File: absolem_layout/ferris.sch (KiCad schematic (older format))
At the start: 100 parts, among them J1 USB C, K0_0 KEYSW, K0_1 KEYSW, K0_2 KEYSW, K0_3 KEYSW, K0_4 KEYSW, K0_5 KEYSW, K0_6 KEYSW, K0_7 KEYSW, K0_8 KEYSW, K0_9 KEYSW, K1_0 KEYSW, K1_1 KEYSW, K1_2 KEYSW, K1_3 KEYSW, K1_4 KEYSW, K1_5 KEYSW, K1_6 KEYSW, K1_7 KEYSW, K1_8 KEYSW, K1_9 KEYSW, K2_0 KEYSW, K2_1 KEYSW, K2_2 KEYSW, K2_3 KEYSW, K2_4 KEYSW, K2_5 KEYSW, K2_6 KEYSW, K2_7 KEYSW, K2_8 KEYSW, K2_9 KEYSW, K3_2 KEYSW, K3_3 KEYSW, K3_4 KEYSW, K3_5 KEYSW, K3_6 KEYSW, K3_7 KEYSW, SW1 SW_PUSH, U1 ATmega32U4-AU, U3 PCA9539PW, Y1 Crystal

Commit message: Fixed some staggering
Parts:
- removed C10, C9: 0.1u, Capacitor_SMD:C_0805_2012Metric_Pad1.15x1.40mm_HandSolder, symbol Device:C_Small
- removed Jack0, Jack1: TRRS, kbd:TRRS-PJ-320A, symbol Connector:AudioJack4
- removed R7, R8: 4.7k, Resistor_SMD:R_0805_2012Metric_Pad1.15x1.40mm_HandSolder, symbol Device:R
- removed R9: 10k, Resistor_SMD:R_0805_2012Metric_Pad1.15x1.40mm_HandSolder, symbol Device:R
- removed U3: PCA9539PW, Package_SO:TSSOP-24_4.4x7.8mm_P0.65mm, symbol ferris-rescue:PCA9539PW-Interface_Expansion-ferris-rescue
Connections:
- wire segments 137 -> 107
- no-connect marks 18 -> 10

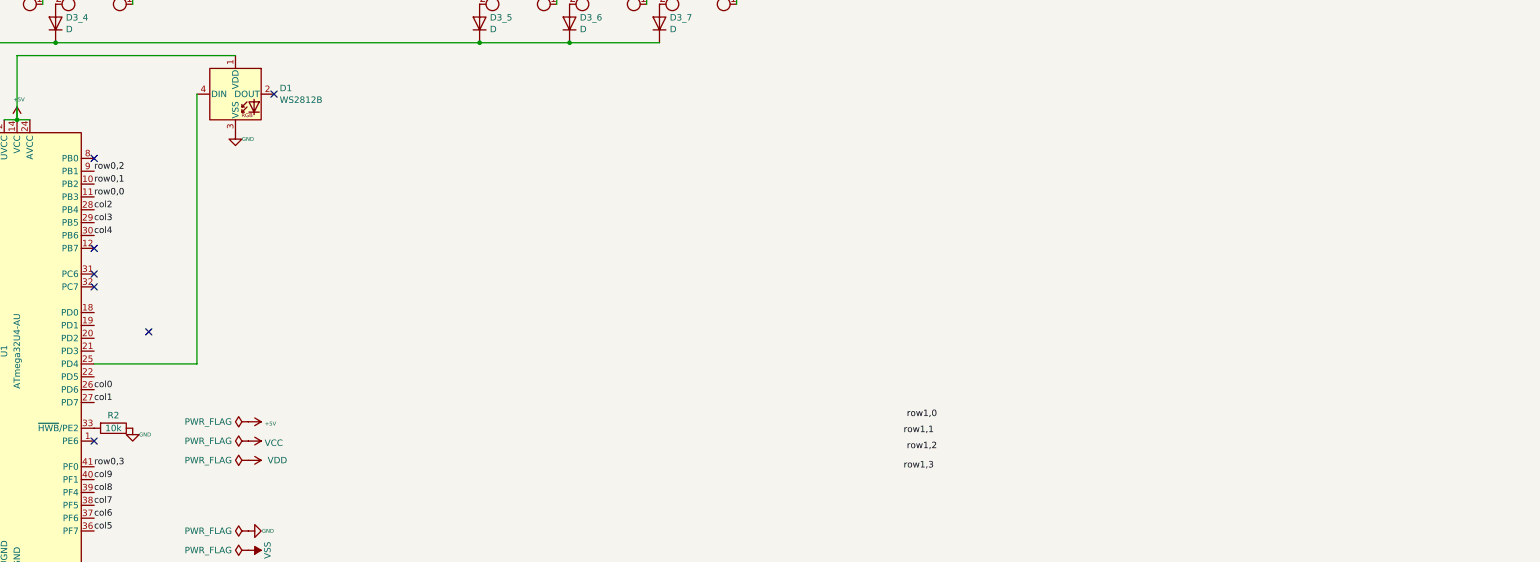
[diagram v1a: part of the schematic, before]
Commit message: Fixed some minor routing and silksscreen
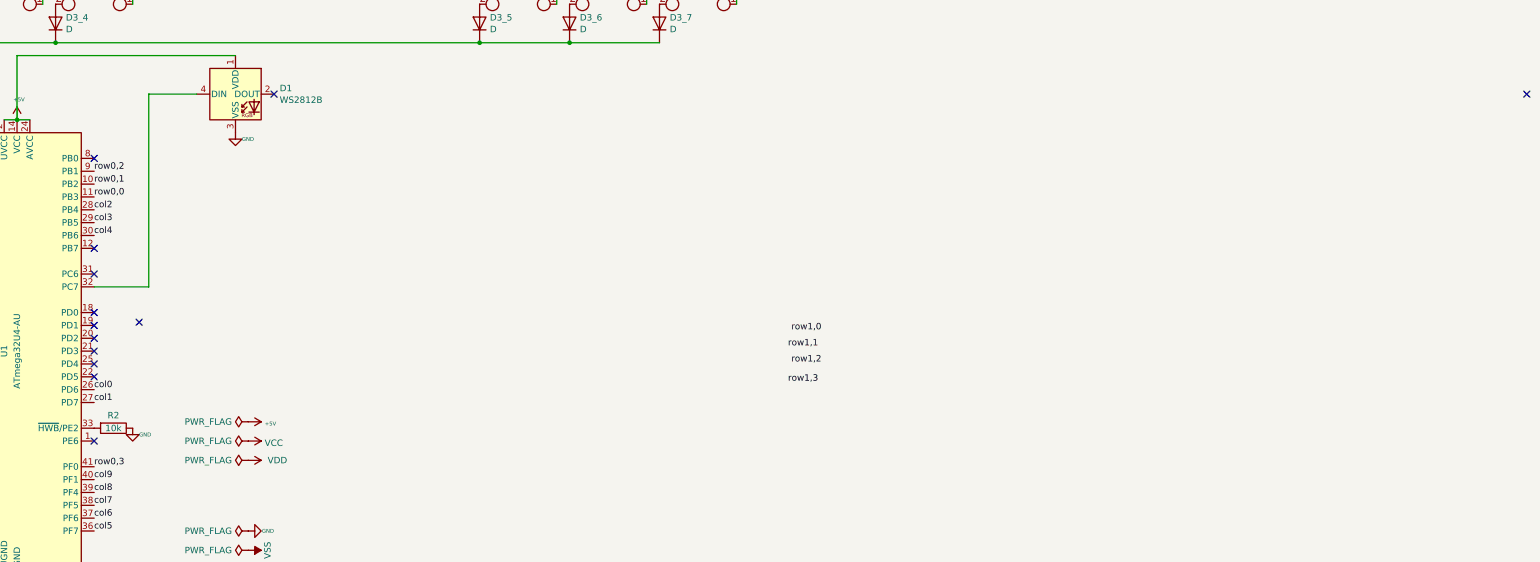
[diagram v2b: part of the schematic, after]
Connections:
- wire segments 107 -> 108
- no-connect marks 10 -> 16
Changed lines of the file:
@@
 	9950 1500 10550 1500
 Connection ~ 9950 1500
-Text Label 10475 6225 0    50   ~ 0
-row1,0
-Text Label 10450 6350 0    50   ~ 0
-row1,1
-Text Label 10475 6475 0    50   ~ 0
-row1,2
-Text Label 10450 6625 0    50   ~ 0
-row1,3
 Text Label 4150 7100 0    50   ~ 0
 col5
@@
 	2350 6000 2450 6000
 Connection ~ 2350 6000
-NoConn ~ 4150 4200
 NoConn ~ 4150 4900
 NoConn ~ 4150 6400
@@
 Text Label 4150 4400 0    50   ~ 0
 row0,1
-Text Label 4150 4300 0    50   ~ 0
-row0,2
 Text Label 4150 6600 0    50   ~ 0
 row0,3
@@
 $EndComp
 NoConn ~ 4150 5100
-NoConn ~ 4150 5200
 Wire Wire Line
 	1850 4800 1850 4900
@@
 $EndComp
 NoConn ~ 5550 3700
-NoConn ~ 4575 5550
 $Comp
 L ferris-rescue:KEYSW-keyboard_parts-ferris-rescue K3_2
@@
 Text Label 4150 6700 0    50   ~ 0
 col9
-Wire Wire Line
-	4150 5800 4950 5800
-Wire Wire Line
-	4950 5800 4950 3700
+NoConn ~ 4500 5475
+Text Label 4150 4300 0    50   ~ 0
+row0,2
+NoConn ~ 4150 4200
+NoConn ~ 15300 3700
+Text Label 9550 5950 0    50   ~ 0
+row1,3
+Text Label 9575 5800 0    50   ~ 0
+row1,2
+Text Label 9550 5675 0    50   ~ 0
+row1,1
+Text Label 9575 5550 0    50   ~ 0
+row1,0
+Wire Wire Line
+	4950 3700 4575 3700
+Wire Wire Line
+	4575 3700 4575 5200
+Wire Wire Line
+	4575 5200 4150 5200
+NoConn ~ 4150 5400
+NoConn ~ 4150 5500
+NoConn ~ 4150 5600
+NoConn ~ 4150 5700
+NoConn ~ 4150 5800
+NoConn ~ 4150 5900
 $EndSCHEMATC

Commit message: Computer change
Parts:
- added C? (x2): 1u, Capacitor_SMD:C_0805_2012Metric_Pad1.15x1.40mm_HandSolder, symbol Device:C_Small
- added IC?: NUF2221W1T2G, SOT-363, symbol NUF2221W1T2G:NUF2221W1T2G
- added U?: TLV70012_SOT23-5, Package_TO_SOT_SMD:SOT-23-5, symbol Regulator_Linear:TLV70012_SOT23-5
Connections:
- net labels added: +3.3V, D+I, D-I
- wire segments 108 -> 123
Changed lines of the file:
@@
 Wire Wire Line
 	7750 900  7750 1200
-Text Label 6750 875  2    50   ~ 0
+Text Label 15200 875  2    50   ~ 0
 row1,0
-Text Label 6750 1000 2    50   ~ 0
+Text Label 15200 1000 2    50   ~ 0
 row1,1
 $Comp
@@
 	1    0    0    -1
 $EndComp
-Text Label 6750 1125 2    50   ~ 0
+Text Label 15200 1125 2    50   ~ 0
 row1,2
 $Comp
@@
 $EndComp
 Text Label 1850 5300 0    50   ~ 0
-D+
+D+I
 Text Label 1850 5200 0    50   ~ 0
-D-
+D-I
 Text Label 2950 5300 2    50   ~ 0
 D-
@@
 	1    0    0    -1
 $EndComp
-Wire Wire Line
-	5250 3400 3550 3400
-Wire Wire Line
-	3550 3400 3550 3900
 $Comp
 L power:GND #PWR0118
@@
 	7850 3300 8550 3300
 Connection ~ 7850 3300
-Text Label 6750 1250 2    50   ~ 0
+Text Label 15200 1250 2    50   ~ 0
 row1,3
 Wire Wire Line
@@
 NoConn ~ 4150 4200
 NoConn ~ 15300 3700
-Text Label 9550 5950 0    50   ~ 0
+Text Label 15500 1250 0    50   ~ 0
 row1,3
-Text Label 9575 5800 0    50   ~ 0
+Text Label 15525 1100 0    50   ~ 0
 row1,2
-Text Label 9550 5675 0    50   ~ 0
+Text Label 15500 975  0    50   ~ 0
 row1,1
-Text Label 9575 5550 0    50   ~ 0
+Text Label 15525 850  0    50   ~ 0
 row1,0
 Wire Wire Line
@@
 NoConn ~ 4150 5800
 NoConn ~ 4150 5900
+Wire Wire Line
+	5250 3400 3800 3400
+Wire Wire Line
+	3800 3400 3800 3900
+Wire Wire Line
+	3800 3900 3650 3900
+Connection ~ 3650 3900
+$Comp
+L NUF2221W1T2G:NUF2221W1T2G IC?
+U 1 1 5F2F5E67
+P 1475 10250
+F 0 "IC?" H 1475 10250 50  0001 L BNN
+F 1 "NUF2221W1T2G" H 1475 10250 50  0001 L BNN
+F 2 "SOT-363" H 1475 10250 50  0001 L BNN
+F 3 "Good" H 1475 10250 50  0001 L BNN
+F 4 "SOT-363 ON Semiconductor" H 1475 10250 50  0001 L BNN "Field4"
+F 5 "NUF2221W1T2G" H 1475 10250 50  0001 L BNN "Field5"
+F 6 "0.27 USD" H 1475 10250 50  0001 L BNN "Field6"
+F 7 "NUF2221W1T2G Series 8 V USB Upstream Terminator with ESD Protection - SC-88" H 1475 10250 50  0001 L BNN "Field7"
+F 8 "ON Semiconductor" H 1475 10250 50  0001 L BNN "Field8"
+	1    1475 10250
+	1    0    0    -1
+$EndComp
+Text Label 1075 10350 2    50   ~ 0
+D+I
+Text Label 1075 10450 2    50   ~ 0
+D-I
+$Comp
+L Regulator_Linear:TLV70012_SOT23-5 U?
+U 1 1 5F305548
+P 3825 9875
+F 0 "U?" H 3825 10217 50  0000 C CNN
+F 1 "TLV70012_SOT23-5" H 3825 10126 50  0000 C CNN
+F 2 "Package_TO_SOT_SMD:SOT-23-5" H 3825 10200 50  0001 C CIN
+F 3 "http://www.ti.com/lit/ds/symlink/tlv700.pdf" H 3825 9925 50  0001 C CNN
+	1    3825 9875
+	1    0    0    -1
+$EndComp
+$Comp
+L power:+5V #PWR?
+U 1 1 5F308B1A
+P 3200 9625
+F 0 "#PWR?" H 3200 9595 20  0001 C CNN
+F 1 "+5V" V 3215 9753 30  0000 L CNN
+F 2 "" H 3200 9625 60  0000 C CNN
+F 3 "" H 3200 9625 60  0000 C CNN
+	1    3200 9625
+	1    0    0    -1
+$EndComp
+$Comp
+L Device:C_Small C?
+U 1 1 5F3097C9
+P 3200 10250
+F 0 "C?" V 3100 10200 50  0000 L CNN
+F 1 "1u" V 3300 10150 50  0000 L CNN
+F 2 "Capacitor_SMD:C_0805_2012Metric_Pad1.15x1.40mm_HandSolder" H 3200 10250 50  0001 C CNN
+F 3 "~" H 3200 10250 50  0001 C CNN
+F 4 "C49678" V 3200 10250 50  0001 C CNN "LCSC Part #"
+	1    3200 10250
+	-1   0    0    1
+$EndComp
+$Comp
+L Device:C_Small C?
+U 1 1 5F30A45A
+P 4500 10225
+F 0 "C?" V 4400 10175 50  0000 L CNN
+F 1 "1u" V 4600 10125 50  0000 L CNN
+F 2 "Capacitor_SMD:C_0805_2012Metric_Pad1.15x1.40mm_HandSolder" H 4500 10225 50  0001 C CNN
+F 3 "~" H 4500 10225 50  0001 C CNN
+F 4 "C49678" V 4500 10225 50  0001 C CNN "LCSC Part #"
+	1    4500 10225
+	1    0    0    -1
+$EndComp
+$Comp
+L power:GND #PWR?
+U 1 1 5F30ABDF
+P 3825 10725
+F 0 "#PWR?" H 3825 10775 20  0001 C CNN
+F 1 "GND" V 3825 10525 30  0000 L CNN
+F 2 "" H 3825 10725 60  0000 C CNN
+F 3 "" H 3825 10725 60  0000 C CNN
+	1    3825 10725
+	1    0    0    -1
+$EndComp
+$Comp
+L power:+3.3V #PWR?
+U 1 1 5F30C6C4
+P 5350 6775
+F 0 "#PWR?" H 5350 6625 50  0001 C CNN
+F 1 "+3.3V" V 5365 6903 50  0000 L CNN
+F 2 "" H 5350 6775 50  0001 C CNN
+F 3 "" H 5350 6775 50  0001 C CNN
+	1    5350 6775
+	0    1    1    0
+$EndComp
+$Comp
+L power:PWR_FLAG #FLG?
+U 1 1 5F30D7CC
+P 5350 6775
+F 0 "#FLG?" H 5350 6850 50  0001 C CNN
+F 1 "PWR_FLAG" V 5350 6902 50  0000 L CNN
+F 2 "" H 5350 6775 50  0001 C CNN
+F 3 "~" H 5350 6775 50  0001 C CNN
+	1    5350 6775
+	0    -1   -1   0
+$EndComp
+$Comp
+L power:+3.3V #PWR?
+U 1 1 5F30EBCB
+P 4500 9625
+F 0 "#PWR?" H 4500 9475 50  0001 C CNN
+F 1 "+3.3V" H 4515 9798 50  0000 C CNN
+F 2 "" H 4500 9625 50  0001 C CNN
+F 3 "" H 4500 9625 50  0001 C CNN
+	1    4500 9625
+	1    0    0    -1
+$EndComp
+Wire Wire Line
+	3825 10175 3825 10500
+Wire Wire Line
+	3200 10350 3200 10500
+Wire Wire Line
+	3200 10500 3825 10500
+Connection ~ 3825 10500
+Wire Wire Line
+	3825 10500 3825 10725
+Wire Wire Line
+	4500 10325 4500 10500
+Wire Wire Line
+	4500 10500 3825 10500
+Wire Wire Line
+	4500 9625 4500 9775
+Wire Wire Line
+	4125 9775 4500 9775
+Connection ~ 4500 9775
+Wire Wire Line
+	4500 9775 4500 10125
+Wire Wire Line
+	3525 9775 3200 9775
+Wire Wire Line
+	3200 9625 3200 9775
+Connection ~ 3200 9775
+Wire Wire Line
+	3200 9775 3200 9875
+Wire Wire Line
+	3525 9875 3200 9875
+Connection ~ 3200 9875
+Wire Wire Line
+	3200 9875 3200 10150
+Text Label 1875 10350 0    50   ~ 0
+D+
+Text Label 1875 10450 0    50   ~ 0
+D-
+$Comp
+L power:+3.3V #PWR?
+U 1 1 5F335F51
+P 1075 10150
+F 0 "#PWR?" H 1075 10000 50  0001 C CNN
+F 1 "+3.3V" V 1090 10278 50  0000 L CNN
+F 2 "" H 1075 10150 50  0001 C CNN
+F 3 "" H 1075 10150 50  0001 C CNN
+	1    1075 10150
+	0    -1   -1   0
+$EndComp
+$Comp
+L power:GND #PWR?
+U 1 1 5F336B78
+P 1075 10650
+F 0 "#PWR?" H 1075 10700 20  0001 C CNN
+F 1 "GND" V 1075 10450 30  0000 L CNN
+F 2 "" H 1075 10650 60  0000 C CNN
+F 3 "" H 1075 10650 60  0000 C CNN
+	1    1075 10650
+	0    1    1    0
+$EndComp
 $EndSCHEMATC

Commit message: Devid commit
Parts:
- added C? (x2): 22p, Capacitor_SMD:C_0805_2012Metric_Pad1.15x1.40mm_HandSolder, symbol Device:C_Small
- added R?: 10k, Resistor_SMD:R_0805_2012Metric_Pad1.15x1.40mm_HandSolder, symbol Device:R
- added SW?: SW_PUSH, Button_Switch_SMD:SW_SPST_B3U-1000P, symbol ferris-rescue:SW_PUSH-keyboard_parts-ferris-rescue
- added U?: STM32F303CBTx, Package_QFP:LQFP-48_7x7mm_P0.5mm, symbol MCU_ST_STM32F3:STM32F303CBTx
- added Y?: Crystal_GND24, symbol Device:Crystal_GND24
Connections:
- net +3V3: now also SW?.1, U?.1 (VBAT), U?.24 (VDD), U?.36 (VDD), U?.48 (VDD), U?.9 (VDDA)
- net GND: now also R?.1, U?.23 (VSS), U?.35 (VSS), U?.47 (VSS), U?.8 (VSSA)
- new net: R?.2, SW?.2, U?.44 (BOOT0)
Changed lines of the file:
@@
 	0    1    1    0
 $EndComp
+$Comp
+L MCU_ST_STM32F3:STM32F303CBTx U?
+U 1 1 5F2CE539
+P 10825 5425
+F 0 "U?" H 10825 5675 50  0000 C CNN
+F 1 "STM32F303CBTx" H 10825 5525 50  0000 C CNN
+F 2 "Package_QFP:LQFP-48_7x7mm_P0.5mm" H 10225 4025 50  0001 R CNN
+F 3 "http://www.st.com/st-web-ui/static/active/en/resource/technical/document/datasheet/DM00058181.pdf" H 10825 5425 50  0001 C CNN
+	1    10825 5425
+	1    0    0    -1
+$EndComp
+$Comp
+L power:+3.3V #PWR?
+U 1 1 5F2D5F54
+P 10825 3500
+F 0 "#PWR?" H 10825 3350 50  0001 C CNN
+F 1 "+3.3V" H 10840 3673 50  0000 C CNN
+F 2 "" H 10825 3500 50  0001 C CNN
+F 3 "" H 10825 3500 50  0001 C CNN
+	1    10825 3500
+	1    0    0    -1
+$EndComp
+Wire Wire Line
+	10825 3925 10825 3650
+Wire Wire Line
+	11025 3925 11025 3650
+Wire Wire Line
+	11025 3650 10925 3650
+Connection ~ 10825 3650
+Wire Wire Line
+	10825 3650 10825 3500
+Wire Wire Line
+	10925 3925 10925 3650
+Connection ~ 10925 3650
+Wire Wire Line
+	10925 3650 10825 3650
+Wire Wire Line
+	10725 3925 10725 3650
+Wire Wire Line
+	10725 3650 10825 3650
+Wire Wire Line
+	10625 3925 10625 3650
+Wire Wire Line
+	10625 3650 10725 3650
+Connection ~ 10725 3650
+$Comp
+L power:GND #PWR?
+U 1 1 5F30895E
+P 10750 7225
+F 0 "#PWR?" H 10750 7275 20  0001 C CNN
+F 1 "GND" V 10750 7025 30  0000 L CNN
+F 2 "" H 10750 7225 60  0000 C CNN
+F 3 "" H 10750 7225 60  0000 C CNN
+	1    10750 7225
+	1    0    0    -1
+$EndComp
+Wire Wire Line
+	10625 6925 10625 7225
+Wire Wire Line
+	10625 7225 10725 7225
+Wire Wire Line
+	10925 6925 10925 7225
+Wire Wire Line
+	10925 7225 10825 7225
+Connection ~ 10750 7225
+Wire Wire Line
+	10725 6925 10725 7225
+Connection ~ 10725 7225
+Wire Wire Line
+	10725 7225 10750 7225
+Wire Wire Line
+	10825 6925 10825 7225
+Connection ~ 10825 7225
+Wire Wire Line
+	10825 7225 10750 7225
+$Comp
+L ferris-rescue:SW_PUSH-keyboard_parts-ferris-rescue SW?
+U 1 1 5F33508A
+P 8650 4325
+F 0 "SW?" H 8650 4325 50  0000 C CNN
+F 1 "SW_PUSH" H 8650 4475 50  0000 C CNN
+F 2 "Button_Switch_SMD:SW_SPST_B3U-1000P" H 8650 4325 60  0001 C CNN
+F 3 "" H 8650 4325 60  0001 C CNN
+F 4 "C231329" H 8650 4325 50  0001 C CNN "LCSC Part #"
+	1    8650 4325
+	1    0    0    -1
+$EndComp
+Wire Wire Line
+	10125 4325 9000 4325
+$Comp
+L power:+3.3V #PWR?
+U 1 1 5F346246
+P 8350 4025
+F 0 "#PWR?" H 8350 3875 50  0001 C CNN
+F 1 "+3.3V" H 8365 4198 50  0000 C CNN
+F 2 "" H 8350 4025 50  0001 C CNN
+F 3 "" H 8350 4025 50  0001 C CNN
+	1    8350 4025
+	1    0    0    -1
+$EndComp
+Wire Wire Line
+	8350 4025 8350 4325
+$Comp
+L Device:R R?
+U 1 1 5F355C69
+P 9000 4475
+F 0 "R?" V 8900 4475 50  0000 C CNN
+F 1 "10k" V 9000 4475 50  0000 C CNN
+F 2 "Resistor_SMD:R_0805_2012Metric_Pad1.15x1.40mm_HandSolder" V 8930 4475 50  0001 C CNN
+F 3 "~" H 9000 4475 50  0001 C CNN
+F 4 "C17414" V 9000 4475 50  0001 C CNN "LCSC Part #"
+	1    9000 4475
+	-1   0    0    1
+$EndComp
+Connection ~ 9000 4325
+Wire Wire Line
+	9000 4325 8950 4325
+$Comp
+L power:GND #PWR?
+U 1 1 5F359ECB
+P 9000 4725
+F 0 "#PWR?" H 9000 4775 20  0001 C CNN
+F 1 "GND" V 9000 4525 30  0000 L CNN
+F 2 "" H 9000 4725 60  0000 C CNN
+F 3 "" H 9000 4725 60  0000 C CNN
+	1    9000 4725
+	1    0    0    -1
+$EndComp
+Wire Wire Line
+	9000 4625 9000 4725
+$Comp
+L Device:Crystal_GND24 Y?
+U 1 1 5F3648C6
+P 6800 8925
+F 0 "Y?" H 6994 8971 50  0000 L CNN
+F 1 "Crystal_GND24" H 6994 8880 50  0000 L CNN
+F 2 "" H 6800 8925 50  0001 C CNN
+F 3 "~" H 6800 8925 50  0001 C CNN
+	1    6800 8925
+	1    0    0    -1
+$EndComp
+$Comp
+L Device:C_Small C?
+U 1 1 5F388BCB
+P 6300 9250
+F 0 "C?" V 6350 9100 50  0000 L CNN
+F 1 "22p" V 6250 9050 50  0000 L CNN
+F 2 "Capacitor_SMD:C_0805_2012Metric_Pad1.15x1.40mm_HandSolder" H 6300 9250 50  0001 C CNN
+F 3 "~" H 6300 9250 50  0001 C CNN
+	1    6300 9250
+	-1   0    0    1
+$EndComp
+$Comp
+L Device:C_Small C?
+U 1 1 5F3901A1
+P 7375 9250
+F 0 "C?" V 7425 9100 50  0000 L CNN
+F 1 "22p" V 7325 9050 50  0000 L CNN
+F 2 "Capacitor_SMD:C_0805_2012Metric_Pad1.15x1.40mm_HandSolder" H 7375 9250 50  0001 C CNN
+F 3 "~" H 7375 9250 50  0001 C CNN
+	1    7375 9250
+	-1   0    0    1
+$EndComp
+$Comp
+L power:GND #PWR?
+U 1 1 5F391618
+P 6300 9600
+F 0 "#PWR?" H 6300 9650 20  0001 C CNN
+F 1 "GND" V 6300 9400 30  0000 L CNN
+F 2 "" H 6300 9600 60  0000 C CNN
+F 3 "" H 6300 9600 60  0000 C CNN
+	1    6300 9600
+	1    0    0    -1
+$EndComp
+$Comp
+L power:GND #PWR?
+U 1 1 5F392713
+P 7375 9625
+F 0 "#PWR?" H 7375 9675 20  0001 C CNN
+F 1 "GND" V 7375 9425 30  0000 L CNN
+F 2 "" H 7375 9625 60  0000 C CNN
+F 3 "" H 7375 9625 60  0000 C CNN
+	1    7375 9625
+	1    0    0    -1
+$EndComp
+$Comp
+L power:GND #PWR?
+U 1 1 5F392D31
+P 6800 9400
+F 0 "#PWR?" H 6800 9450 20  0001 C CNN
+F 1 "GND" V 6800 9200 30  0000 L CNN
+F 2 "" H 6800 9400 60  0000 C CNN
+F 3 "" H 6800 9400 60  0000 C CNN
+	1    6800 9400
+	1    0    0    -1
+$EndComp
 $EndSCHEMATC
